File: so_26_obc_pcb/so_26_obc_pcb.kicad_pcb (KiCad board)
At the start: 2 copper layers, 90.2 x 95.9 mm, 41 parts, among them J1 Conn_02x12_Odd_Even, J2 Conn_02x06_Odd_Even, J3 Conn_01x04, J4 Conn_01x03, J5 Conn_01x03, SW1 SW_Push, U1 STM32G431RBTx, U2 MPRLS0025, U3 PCT2075, U4 LSM6DS3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

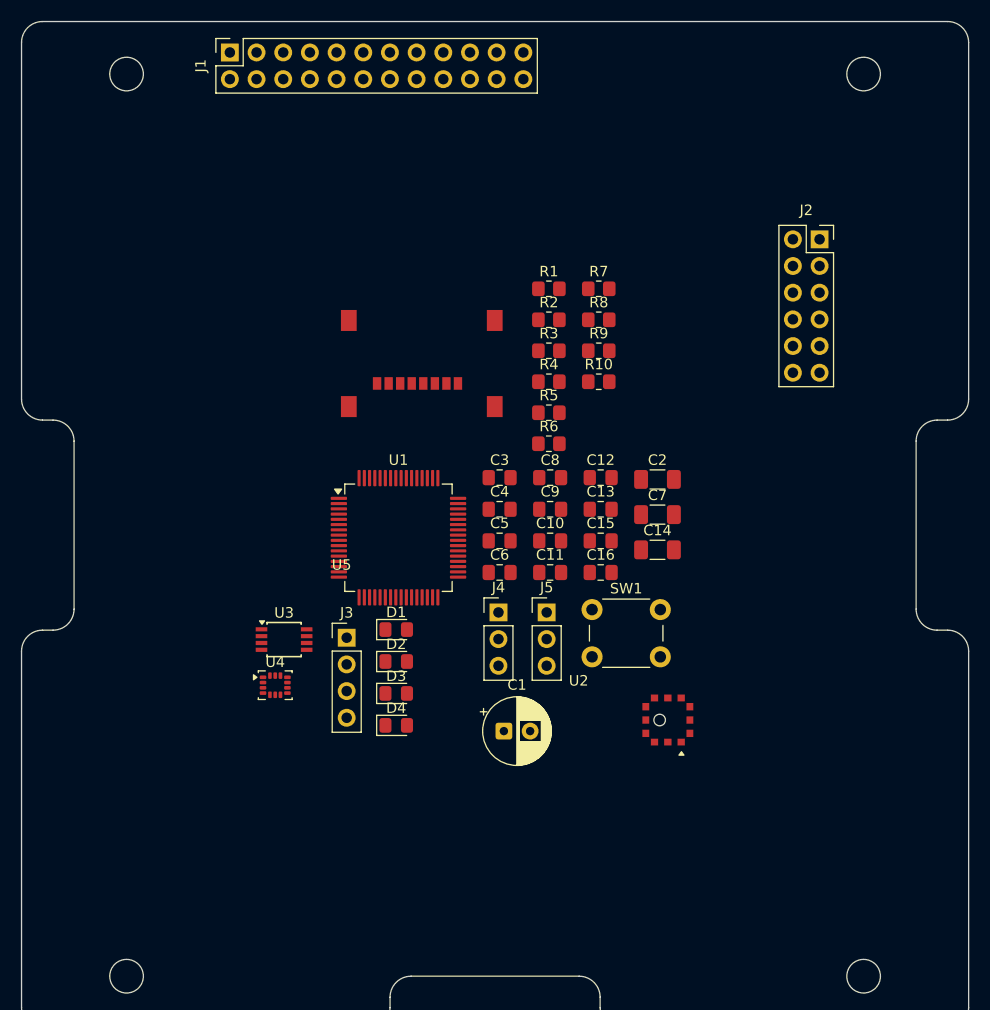
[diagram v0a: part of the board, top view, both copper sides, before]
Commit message: Schematic: added low_power_mode
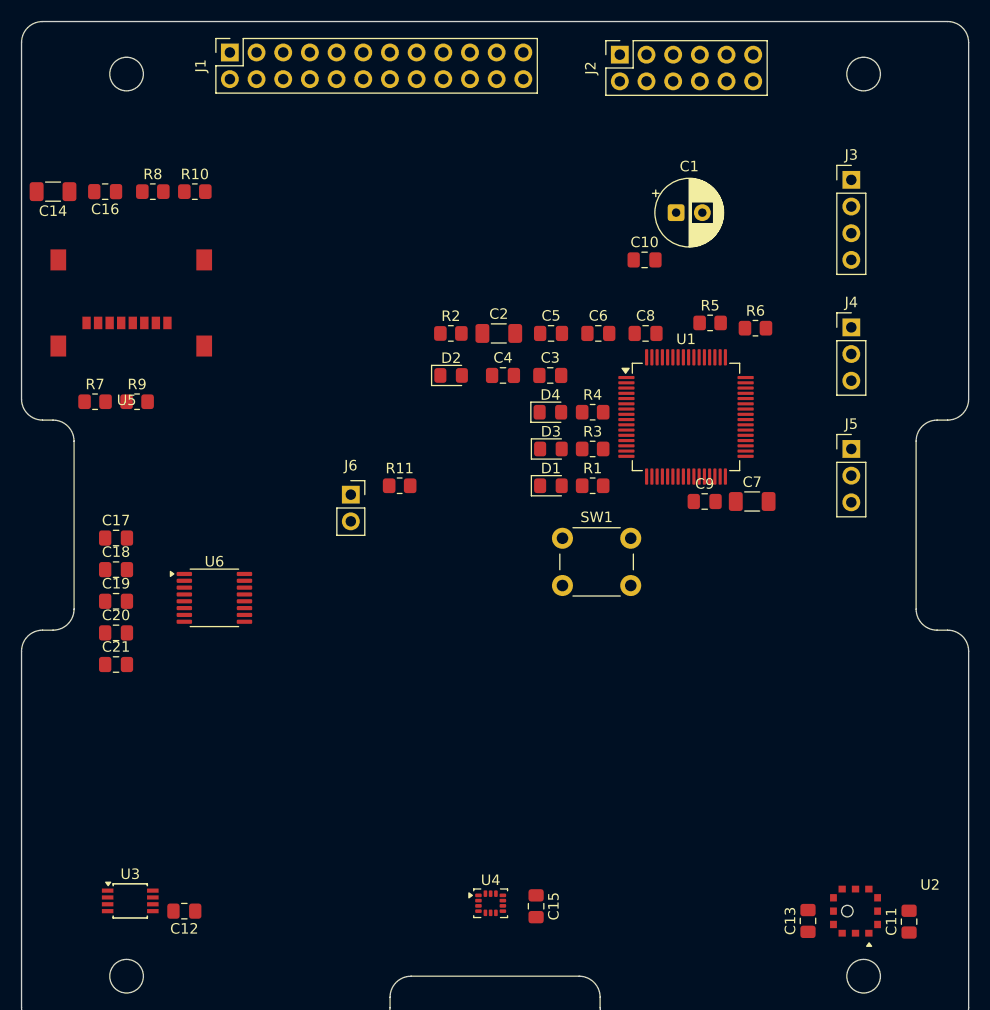
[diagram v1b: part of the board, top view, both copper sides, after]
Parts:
- added C17: 100n, Capacitor_SMD:C_0805_2012Metric_Pad1.18x1.45mm_HandSolder, F.Cu at (65.0, 94.5)
- added C18: 100n, Capacitor_SMD:C_0805_2012Metric_Pad1.18x1.45mm_HandSolder, F.Cu at (65.0, 97.5)
- added C19: 100n, Capacitor_SMD:C_0805_2012Metric_Pad1.18x1.45mm_HandSolder, F.Cu at (65.0, 100.5)
- added C20: 100n, Capacitor_SMD:C_0805_2012Metric_Pad1.18x1.45mm_HandSolder, F.Cu at (65.0, 103.5)
- added C21: 100n, Capacitor_SMD:C_0805_2012Metric_Pad1.18x1.45mm_HandSolder, F.Cu at (65.0, 106.5)
- added J6: Conn_01x02, Connector_PinSocket_2.54mm:PinSocket_1x02_P2.54mm_Vertical, F.Cu at (87.3, 90.3)
- added R11: 10k, Resistor_SMD:R_0805_2012Metric_Pad1.20x1.40mm_HandSolder, F.Cu at (92.0, 89.5)
- added U6: TPT3232A-TS3R, Package_SO:TSSOP-16_4.4x5mm_P0.65mm, F.Cu at (74.4, 100.2)
- moved C14 66.9 mm to (59.0, 61.5), turned to 180 degrees
- moved J3 64.9 mm to (135.0, 60.4)
- moved C16 59.5 mm to (64.0, 61.5), turned to 180 degrees
- moved C12 57.2 mm to (71.5, 130.0), turned to 180 degrees
- moved C1 52.0 mm to (118.3, 63.5)
- moved R7 49.1 mm to (63.0, 81.5)
- moved C11 47.7 mm to (140.5, 131.0), turned to 90 degrees
- moved R9 44.2 mm to (67.0, 81.5)
- moved R8 44.2 mm to (68.5, 61.5)
- moved C13 43.9 mm to (130.9, 130.9), turned to 90 degrees
- moved J4 43.2 mm to (135.0, 74.4)
- moved R10 42.5 mm to (72.5, 61.5)
- moved C15 35.3 mm to (105.0, 129.5), turned to -90 degrees
- moved D4 33.2 mm to (106.3, 82.5)
- moved J5 32.9 mm to (135.0, 86.0)
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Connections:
- J2 pad 4: unconnected-(J2-Pin_4-Pad4) -> ALT_+10V
- U1 pad 43: unconnected-(U1-PA9-Pad43) -> /LOW_POWER_MODE

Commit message: PCB: changed settings to match specs from JCL
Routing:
- added copper zone on In1.Cu, net GND
- added copper zone on In2.Cu, net GND
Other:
- copper layers 2 -> 4
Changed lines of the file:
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@@
 	(layers
 		(0 "F.Cu" signal)
+		(4 "In1.Cu" signal)
+		(6 "In2.Cu" signal)
 		(2 "B.Cu" signal)
 		(9 "F.Adhes" user "F.Adhesive")
@@
 	)
 	(setup
+		(stackup
+			(layer "F.SilkS"
+				(type "Top Silk Screen")
+			)
+			(layer "F.Paste"
+				(type "Top Solder Paste")
+			)
+			(layer "F.Mask"
+				(type "Top Solder Mask")
+				(thickness 0.01)
+			)
+			(layer "F.Cu"
+				(type "copper")
+				(thickness 0.035)
+			)
+			(layer "dielectric 1"
+				(type "prepreg")
+				(thickness 0.1)
+				(material "FR4")
+				(epsilon_r 4.5)
+				(loss_tangent 0.02)
+			)
+			(layer "In1.Cu"
+				(type "copper")
+				(thickness 0.035)
+			)
+			(layer "dielectric 2"
+				(type "core")
+				(thickness 1.24)
+				(material "FR4")
+				(epsilon_r 4.5)
+				(loss_tangent 0.02)
+			)
+			(layer "In2.Cu"
+				(type "copper")
+				(thickness 0.035)
+			)
+			(layer "dielectric 3"
+				(type "prepreg")
+				(thickness 0.1)
+				(material "FR4")
+				(epsilon_r 4.5)
+				(loss_tangent 0.02)
+			)
+			(layer "B.Cu"
+				(type "copper")
+				(thickness 0.035)
+			)
+			(layer "B.Mask"
+				(type "Bottom Solder Mask")
+				(thickness 0.01)
+			)
+			(layer "B.Paste"
+				(type "Bottom Solder Paste")
+			)
+			(layer "B.SilkS"
+				(type "Bottom Silk Screen")
+			)
+			(copper_finish "None")
+			(dielectric_constraints no)
+		)
 		(pad_to_mask_clearance 0)
 		(allow_soldermask_bridges_in_footprints no)
 		(tenting front back)
+		(aux_axis_origin 56 141.2)
+		(grid_origin 56 141.2)
 		(pcbplotparams
 			(layerselection 0x00000000_00000000_55555555_5755f5ff)
@@
 		(layer "Edge.Cuts")
 	)
+	(zone
+		(net 2)
+		(net_name "GND")
+		(layers "In1.Cu" "In2.Cu")
+		(name "GND")
+		(hatch edge 0.5)
+		(connect_pads
+			(clearance 0.3)
+		)
+		(min_thickness 0.25)
+		(filled_areas_thickness no)
+		(fill yes
+			(thermal_gap 0.5)
+			(thermal_bridge_width 0.5)
+		)
+		(polygon
+			(pts
+				(xy 148 42.5) (xy 148 143) (xy 51 143) (xy 51.5 42.5)
+			)
+		)
+	)
 	(group ""

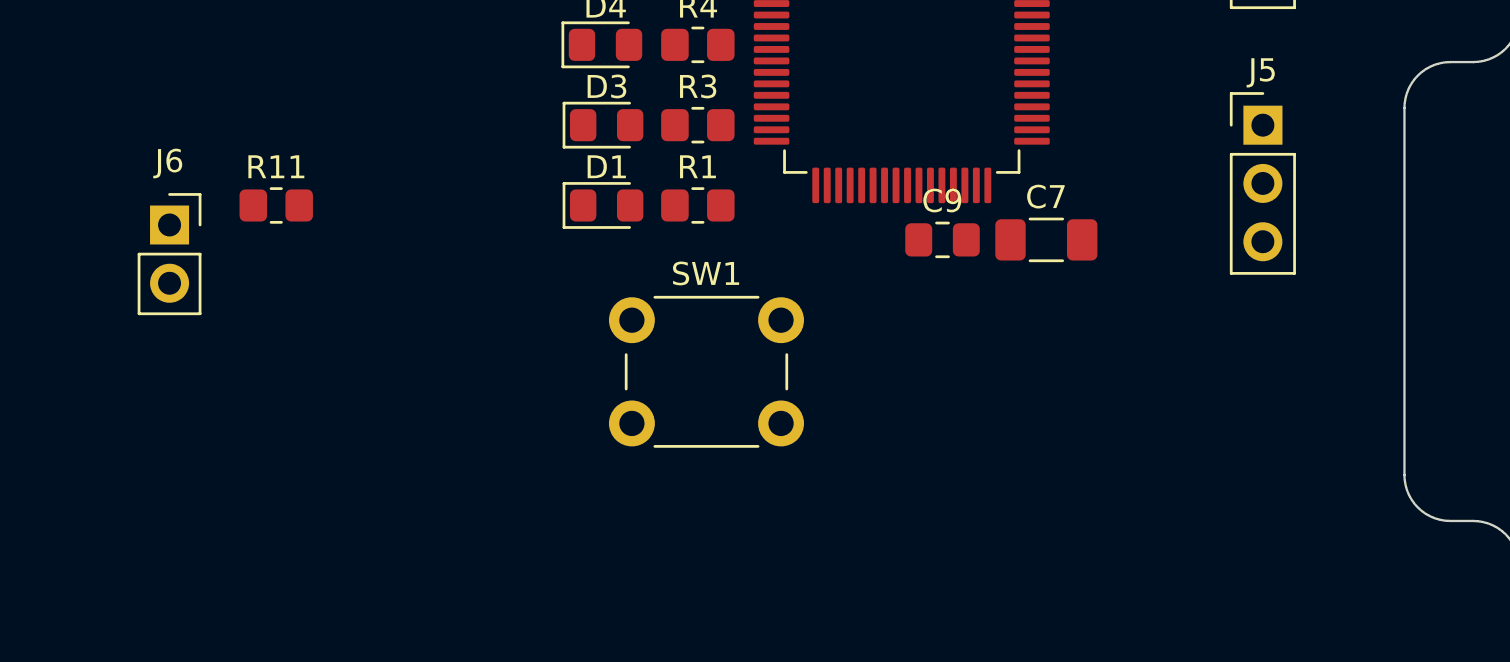
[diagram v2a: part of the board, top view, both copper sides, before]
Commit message: Schematic: Updated level shifter symbol
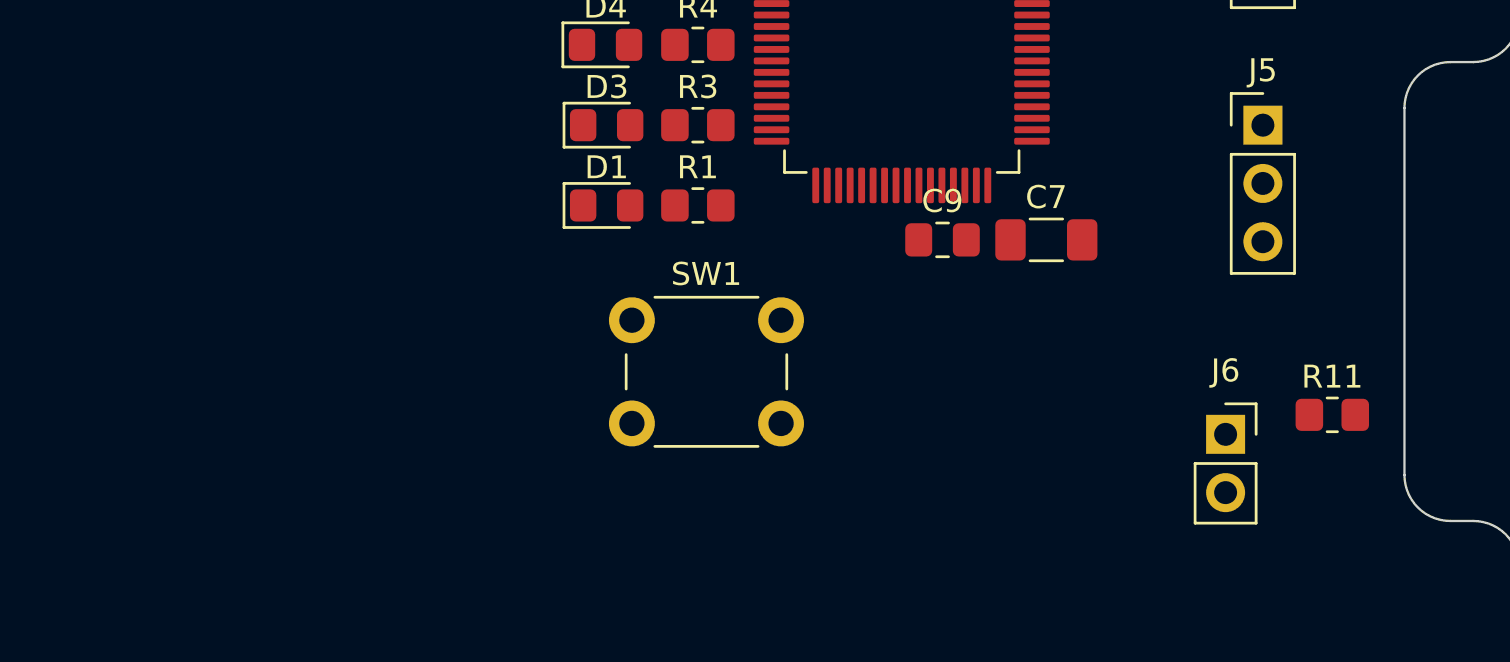
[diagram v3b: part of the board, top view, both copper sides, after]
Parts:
- moved J6 46.9 mm to (133.4, 99.5)
- moved R11 46.9 mm to (138.0, 98.6)
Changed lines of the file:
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@@
 	(footprint "Resistor_SMD:R_0805_2012Metric_Pad1.20x1.40mm_HandSolder"
 		(layer "F.Cu")
-		(at 92 89.5)
+		(at 138.025 98.625)
 		(descr "Resistor SMD 0805 (2012 Metric), square (rectangular) end terminal, IPC-7351 nominal with elongated pad for handsoldering. (Body size source: IPC-SM-782 page 72, https://www.pcb-3d.com/wordpress/wp-content/uploads/ipc-sm-782a_amendment_1_and_2.pdf), generated with kicad-footprint-generator")
 		(tags "resistor handsolder")
@@
 	(footprint "Connector_PinSocket_2.54mm:PinSocket_1x02_P2.54mm_Vertical"
 		(layer "F.Cu")
-		(at 87.35 90.35)
+		(at 133.375 99.475)
 		(descr "Through hole straight socket strip, 1x02, 2.54mm pitch, single row (from Kicad 4.0.7), script generated")
 		(tags "Through hole socket strip THT 1x02 2.54mm single row")

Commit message: review by aj
added max232cpe and other things
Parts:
- added C22: 100n, Capacitor_SMD:C_0805_2012Metric_Pad1.18x1.45mm_HandSolder, F.Cu at (88.0, 111.7)
- added C23: 1u, Capacitor_SMD:C_0805_2012Metric_Pad1.18x1.45mm_HandSolder, F.Cu at (91.0, 111.7)
- added C24: 1u, Capacitor_SMD:C_0805_2012Metric_Pad1.18x1.45mm_HandSolder, F.Cu at (94.0, 111.7)
- added C25: 1u, Capacitor_SMD:C_0805_2012Metric_Pad1.18x1.45mm_HandSolder, F.Cu at (97.0, 111.7)
- added C26: 1u, Capacitor_SMD:C_0805_2012Metric_Pad1.18x1.45mm_HandSolder, F.Cu at (100.1, 111.7)
- added C27: 10u, Capacitor_SMD:C_0805_2012Metric_Pad1.18x1.45mm_HandSolder, F.Cu at (103.1, 111.7)
- added C28: 10u, Capacitor_SMD:C_0805_2012Metric_Pad1.18x1.45mm_HandSolder, F.Cu at (106.1, 111.7)
- added D5: LED_PWR, LED_SMD:LED_0805_2012Metric_Pad1.15x1.40mm_HandSolder, F.Cu at (138.7, 115.0)
- added JP1: SolderJumper_3_Open, Jumper:SolderJumper-3_P1.3mm_Open_Pad1.0x1.5mm, F.Cu at (126.6, 114.8)
- added JP2: SolderJumper_3_Open, Jumper:SolderJumper-3_P1.3mm_Open_Pad1.0x1.5mm, F.Cu at (126.6, 118.6)
- added R12: 10k, Resistor_SMD:R_0805_2012Metric_Pad1.20x1.40mm_HandSolder, F.Cu at (138.6, 118.0)
- added U7: AMS1117-5.0, Package_TO_SOT_SMD:SOT-223-3_TabPin2, F.Cu at (90.7, 104.4)
- added U8: MAX232, Package_DIP:DIP-16_W7.62mm, F.Cu at (88.6, 123.3)
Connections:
- U1 pad 22: /RADIO_TX -> /RADIO_UART_TX
- U1 pad 23: /RADIO_RX -> /RADIO_UART_RX
